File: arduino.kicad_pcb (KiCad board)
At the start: 2 copper layers, 101.6 x 53.3 mm, 76 parts, among them J1 USB_A, J10 7SEL, J11 PA, J12 PB, J13 PC, J14 PD, J15 MICROWIRE, J16 ISP, J17 POWER, J2 NE7555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

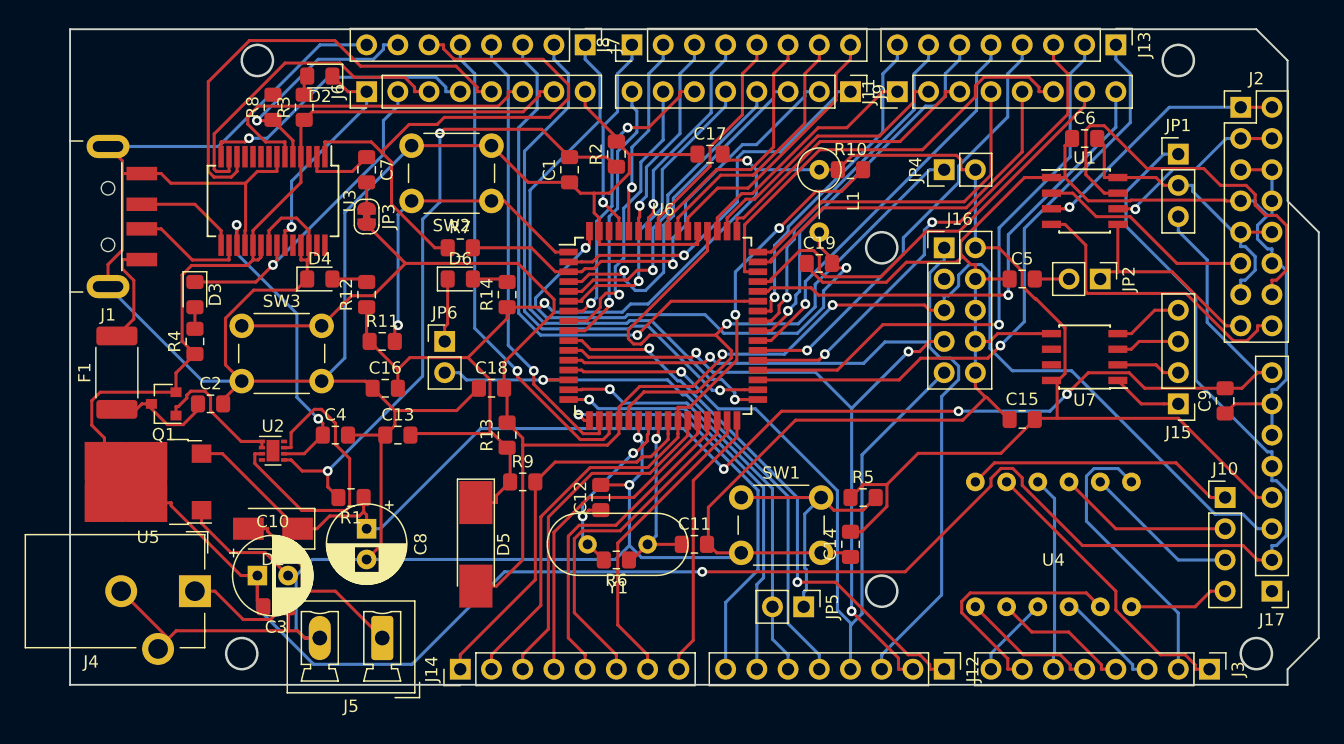
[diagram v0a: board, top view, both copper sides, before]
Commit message: After a night of Freerouting optimization.
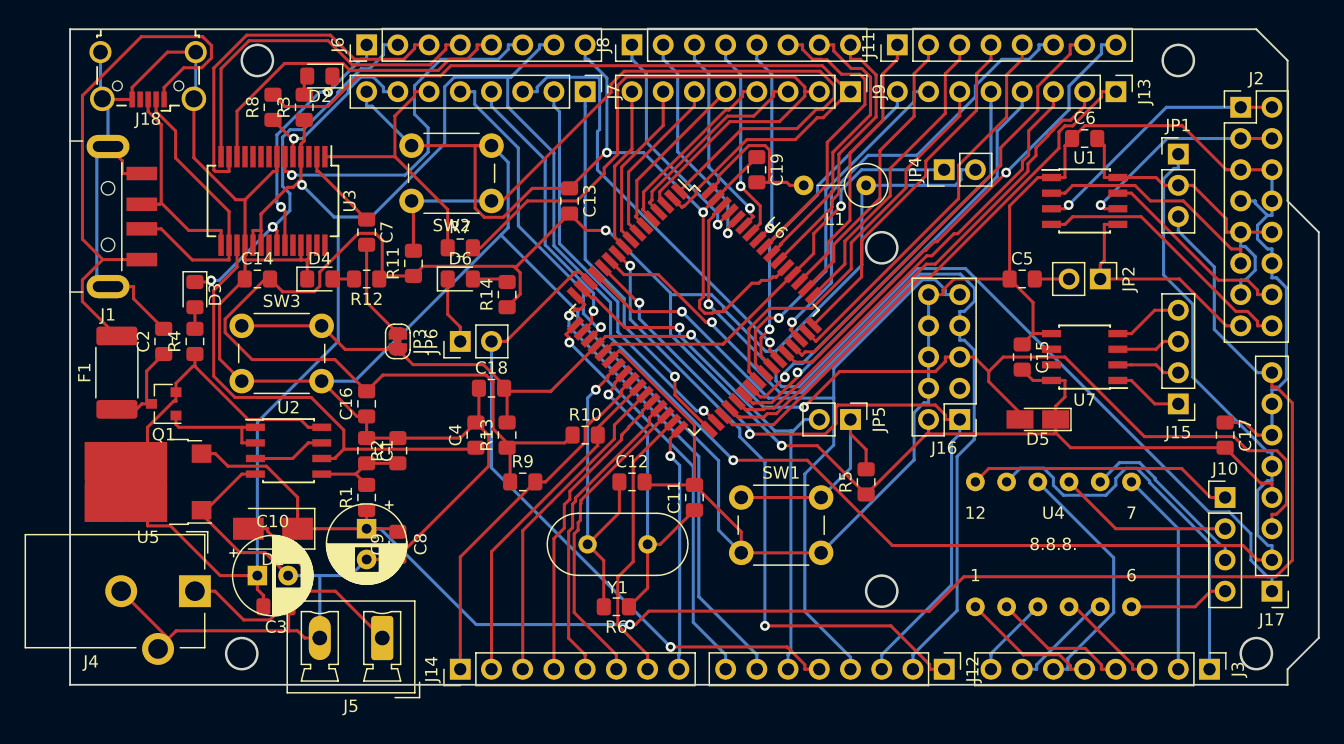
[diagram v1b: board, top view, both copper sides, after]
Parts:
- added J18: USB_B_Micro, Connector_USB:USB_Micro-B_Wuerth_629105150521_CircularHoles, F.Cu at (44.5, 92.7)
- C1, C9: value C -> 100n
- C10, C8: value CP -> 47u
- C11, C12: value C -> 22p
- C13, C14, C15, C16, C17, C2, C4: value C -> C 100n
- C18: value C -> 1u
- C19: value C -> 0.1m
- D1: value D -> M7
- D5: value D -> 4148; footprint Diode_SMD:D_MELF_Handsoldering -> Diode_SMD:D_MicroMELF_Hadsoldering
- R1, R10, R11, R13, R2, R5, R9: value R -> 10k
- R12, R14, R3, R4: value R -> 1k
- R6: value R -> 1M
- R7, R8: value R -> R 1k
- U2: value LM358_DFN -> LM358; footprint Package_DFN_QFN:DFN-8-1EP_2x2mm_P0.5mm_EP1.05x1.75mm -> Package_SO:SOIC-8_3.9x4.9mm_P1.27mm
- moved C9 68.3 mm to (64.8, 130.8)
- moved C14 52.9 mm to (53.3, 109.2), turned to 0 degrees
- moved C17 47.7 mm to (132.1, 121.9), turned to 270 degrees
- moved D5 46.8 mm to (116.8, 120.7), turned to 180 degrees
- moved R10 30.5 mm to (80.0, 121.9)
- moved R2 30.0 mm to (64.8, 123.2)
- moved C1 28.2 mm to (62.2, 123.2), turned to 270 degrees
- moved C13 23.6 mm to (78.7, 102.9), turned to 270 degrees
- moved JP5 15.7 mm to (101.6, 120.7)
- moved J16 14.0 mm to (110.5, 120.7), turned to 180 degrees
- moved C4 11.4 mm to (71.1, 121.9), turned to 90 degrees
- moved JP3 10.5 mm to (64.8, 114.3)
- moved C19 9.16 mm to (94.0, 100.3), turned to 270 degrees
- moved R11 6.84 mm to (66.0, 108.0), turned to 90 degrees
- moved C2 6.35 mm to (45.7, 114.3), turned to 90 degrees
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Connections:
- net Net-(F1-Pad2) renamed usbvbus
- J17 pad 1: (no net) -> aref
- J9 pad 1: rdx -> rxd
- R8 pad 2: (no net) -> rxd
- U2 pad 4: (no net) -> NEGND
- U2 pad 8: (no net) -> +5V
- U6 pad 2: rdx -> rxd
- U6 pad 62: (no net) -> aref
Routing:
- net aref: track 0.00 -> 74.4 mm, vias 0 -> 1
- net rxd: track 0.00 -> 68.5 mm
- net cmp: track 53.5 -> 7.80 mm, vias 2 -> 0
- net VCC: track 160.9 -> 202.0 mm
- net usbvbus: track 8.74 -> 44.9 mm
- net npen: track 26.5 -> 60.5 mm, vias 1 -> 0
- net reset: track 143.9 -> 111.8 mm
- net rdx: track 31.0 -> 0.00 mm, vias 1 -> 0
- net sda: track 57.8 -> 27.9 mm, vias 2 -> 0
- net avcc: track 41.6 -> 13.4 mm, vias 2 -> 0
- net m8txd: track 47.8 -> 22.0 mm
- net Net-(JP4-Pad1): track 57.7 -> 35.7 mm
- net +5V: track 230.1 -> 249.7 mm, vias 1 -> 2
- net Net-(U2-Pad3): track 24.7 -> 5.93 mm
- net NEDIS: track 33.6 -> 16.2 mm
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
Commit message: Added NPN transistor
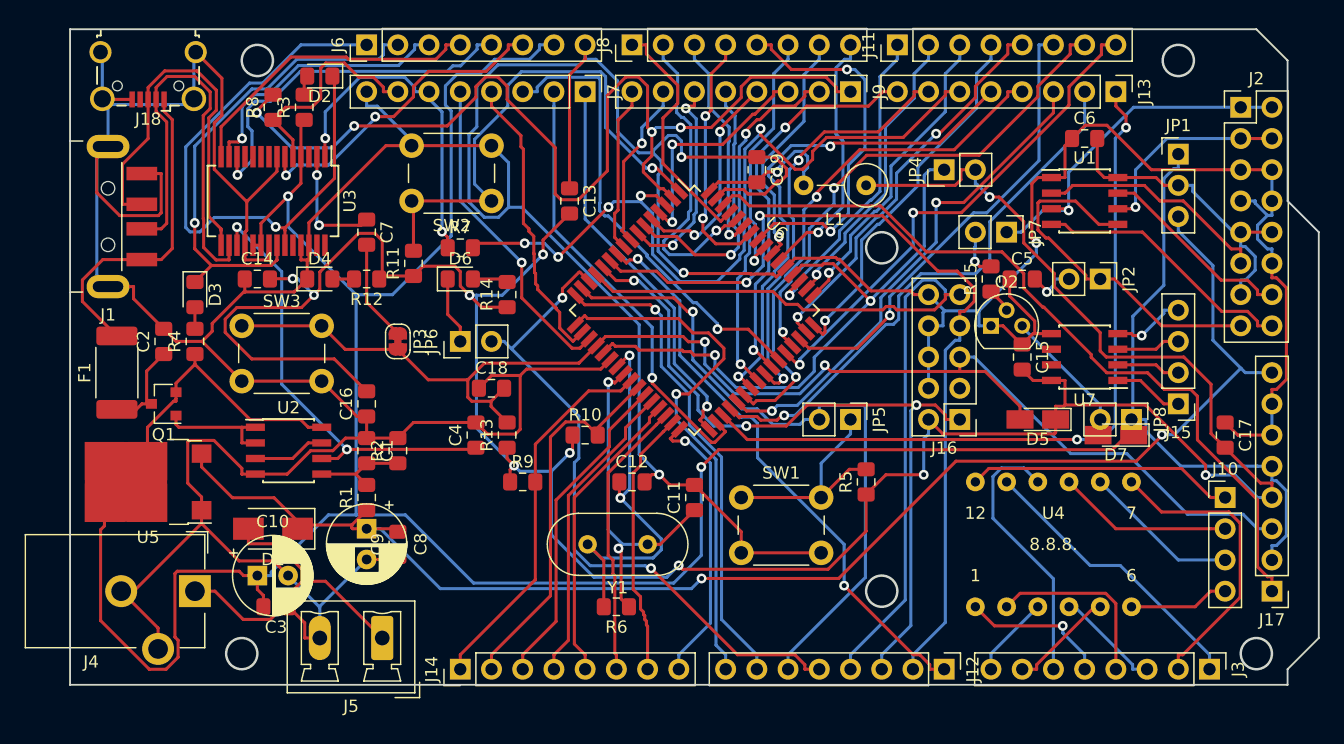
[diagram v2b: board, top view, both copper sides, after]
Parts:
- added D7: 4148, Diode_SMD:D_MicroMELF_Hadsoldering, F.Cu at (123.2, 121.9)
- added JP7: NPN, Connector_PinHeader_2.54mm:PinHeader_1x02_P2.54mm_Vertical, F.Cu at (114.3, 105.4)
- added JP8: RELAY, Connector_PinHeader_2.54mm:PinHeader_1x02_P2.54mm_Vertical, F.Cu at (124.5, 120.7)
- added Q2: 2N3903, Package_TO_SOT_THT:TO-92, F.Cu at (113.0, 113.0)
- added R15: 1k, Resistor_SMD:R_0805_2012Metric_Pad1.15x1.40mm_HandSolder, F.Cu at (113.0, 109.2)
- U4: value CC56-12CGKWA -> MT30361
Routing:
- net NEGND: track 449.1 -> 488.9 mm, vias 2 -> 4
- net cbus0: track 21.7 -> 49.3 mm, vias 2 -> 1
- net VCC: track 202.0 -> 226.4 mm, vias 2 -> 10
- net +5V: track 249.7 -> 273.9 mm
- net usbvbus: track 44.9 -> 26.5 mm
- net npen: track 60.5 -> 42.5 mm, vias 0 -> 1
- net Net-(J13-Pad1): track 44.5 -> 61.0 mm, vias 0 -> 2
- net vin: track 135.0 -> 119.3 mm, vias 1 -> 2
- net Net-(J1-Pad3): track 17.5 -> 32.0 mm
- net rxd: track 68.5 -> 82.8 mm, vias 0 -> 4
- net Net-(JP4-Pad1): track 35.7 -> 49.5 mm, vias 1 -> 2
- net Net-(J8-Pad5): track 16.8 -> 30.4 mm, vias 1 -> 2
- net Net-(J1-Pad2): track 23.7 -> 35.5 mm
- net Net-(D7-Pad2): track 0.00 -> 11.6 mm
- net pb5: track 44.3 -> 55.3 mm
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
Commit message: Routed
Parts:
- C2, C4: value C 100n -> 100n
- C3, C7: value C -> 0.1u
- F1: value Fuse -> 0.5RST
- JP3: value Jumper -> AVR
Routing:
- net +5V: track 273.9 -> 229.4 mm, vias 2 -> 1
- net NEGND: track 488.9 -> 448.7 mm, vias 4 -> 1
- net aref: track 65.1 -> 94.6 mm
- net VCC: track 226.4 -> 199.2 mm, vias 10 -> 1
- net reset: track 112.8 -> 137.5 mm, vias 2 -> 1
- net cbus0: track 49.3 -> 29.8 mm, vias 1 -> 2
- net vin: track 119.3 -> 135.2 mm, vias 2 -> 1
- net Net-(J13-Pad1): track 61.0 -> 45.2 mm, vias 2 -> 0
- net Net-(JP4-Pad1): track 49.5 -> 34.7 mm, vias 2 -> 0
- net Net-(J1-Pad3): track 32.0 -> 17.5 mm
- net Net-(J8-Pad5): track 30.4 -> 16.8 mm, vias 2 -> 1
- net Net-(J1-Pad2): track 35.5 -> 23.7 mm
- net Net-(J3-Pad7): track 8.67 -> 20.3 mm
- net pb5: track 55.3 -> 44.1 mm
- net NECTRLV: track 29.5 -> 18.6 mm
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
